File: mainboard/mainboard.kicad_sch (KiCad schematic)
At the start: 5 parts

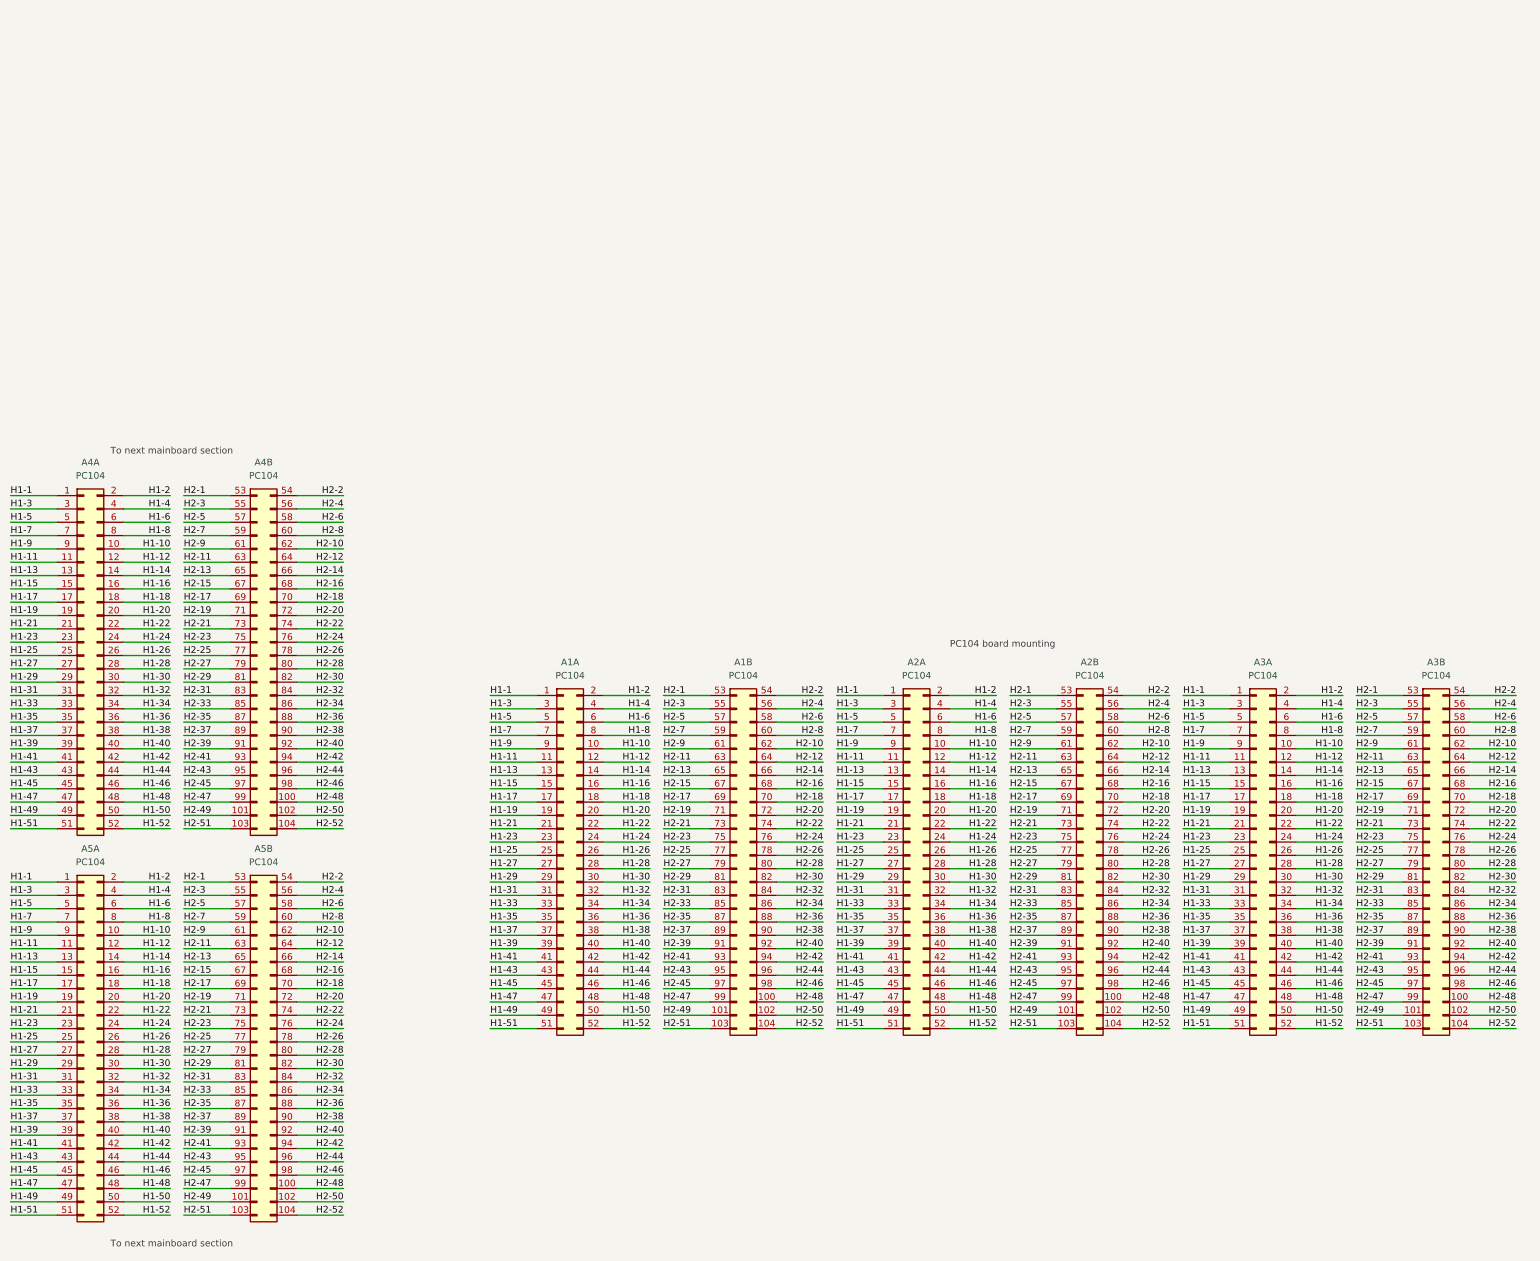
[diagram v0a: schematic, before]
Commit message: lay out the PC104 boards
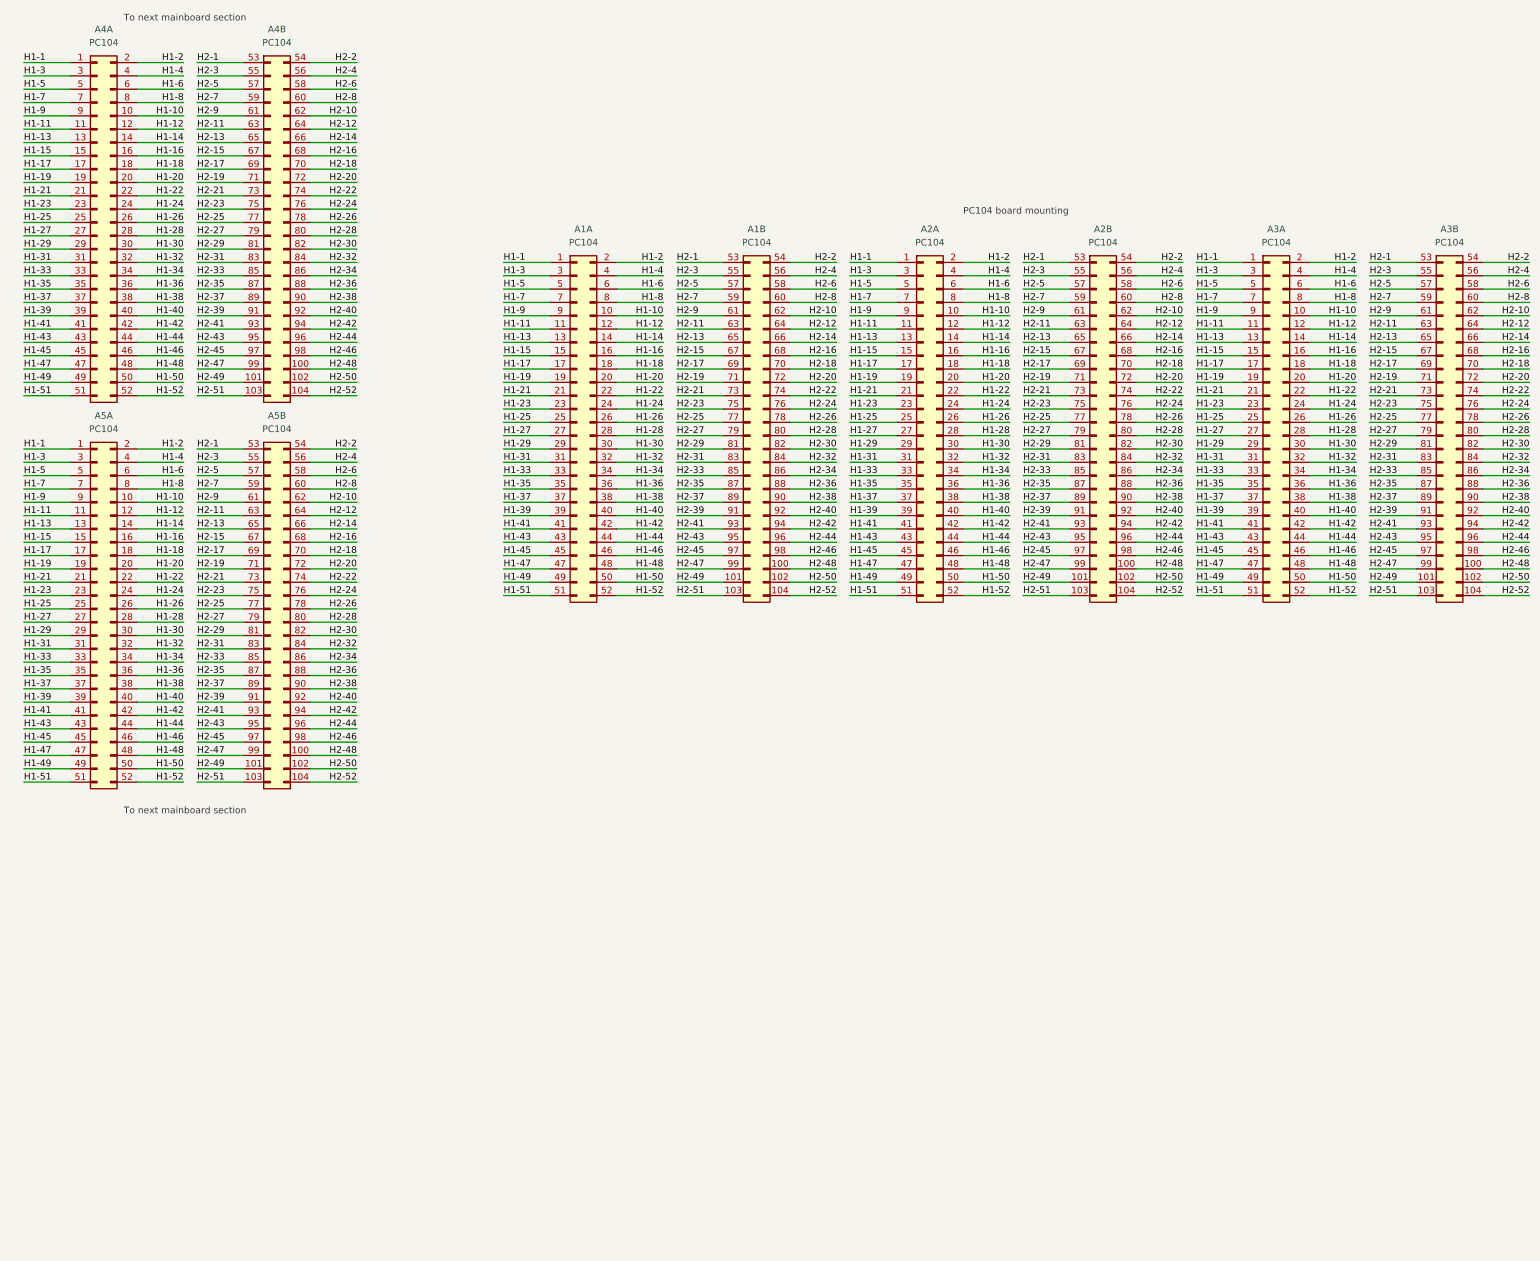
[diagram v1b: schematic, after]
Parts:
- A1, A2, A3: footprint (none) -> flatsat:PC104
- A4, A5: footprint (none) -> flatsat:Header
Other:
- moved on the sheet: A1A, A1B, A2A, A2B, A3A, A3B, A4A, A4B, A5A, A5B

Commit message: grounding
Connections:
- net H2-17 is gone; now on net GND: A1.69 (Pin_17), A2.69 (Pin_17), A3.69 (Pin_17), A4.69 (Pin_17), A5.69 (Pin_17)
- net H2-21 is gone; now on net GND: A1.73 (Pin_21), A2.73 (Pin_21), A3.73 (Pin_21), A4.73 (Pin_21), A5.73 (Pin_21)
- net H2-22 is gone; now on net GND: A1.74 (Pin_22), A2.74 (Pin_22), A3.74 (Pin_22), A4.74 (Pin_22), A5.74 (Pin_22)
- net H2-29 is gone; now on net GND: A1.81 (Pin_29), A2.81 (Pin_29), A3.81 (Pin_29), A4.81 (Pin_29), A5.81 (Pin_29)
- net H2-30 is gone; now on net GND: A1.82 (Pin_30), A2.82 (Pin_30), A3.82 (Pin_30), A4.82 (Pin_30), A5.82 (Pin_30)
- net H2-32 is gone; now on net GND: A1.84 (Pin_32), A2.84 (Pin_32), A3.84 (Pin_32), A4.84 (Pin_32), A5.84 (Pin_32)
- net H2-47 is gone; now on net GND: A1.99 (Pin_47), A2.99 (Pin_47), A3.99 (Pin_47), A4.99 (Pin_47), A5.99 (Pin_47)
- net H2-48 is gone; now on net GND: A1.100 (Pin_48), A2.100 (Pin_48), A3.100 (Pin_48), A4.100 (Pin_48), A5.100 (Pin_48)
- net H2-9 is gone; now on net GND: A1.61 (Pin_9), A2.61 (Pin_9), A3.61 (Pin_9), A4.61 (Pin_9), A5.61 (Pin_9)
- net H2-14 renamed GND

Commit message: bus power flags, finish left side routing
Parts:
- added H1, H2: MountingHole, MountingHole:MountingHole_3.2mm_M3, symbol Mechanical:MountingHole
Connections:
- net H2-26 is gone; now on net +5V: A1.78 (Pin_26), A2.78 (Pin_26), A3.78 (Pin_26), A4.78 (Pin_26), A5.78 (Pin_26)
- net H2-28 is gone; now on net +3V3: A1.80 (Pin_28), A2.80 (Pin_28), A3.80 (Pin_28), A4.80 (Pin_28), A5.80 (Pin_28)
- net H2-46 is gone; now on net +BATT: A1.98 (Pin_46), A2.98 (Pin_46), A3.98 (Pin_46), A4.98 (Pin_46), A5.98 (Pin_46)
- net GND: no longer A1.100 (Pin_48), A1.61 (Pin_9), A1.66 (Pin_14), A1.69 (Pin_17), A1.73 (Pin_21), A1.74 (Pin_22), A1.99 (Pin_47), A2.100 (Pin_48), A2.61 (Pin_9), A2.66 (Pin_14), A2.69 (Pin_17), A2.73 (Pin_21), A2.74 (Pin_22), A2.99 (Pin_47), A3.100 (Pin_48), A3.61 (Pin_9), A3.66 (Pin_14), A3.69 (Pin_17), A3.73 (Pin_21), A3.74 (Pin_22), A3.99 (Pin_47), A4.100 (Pin_48), A4.61 (Pin_9), A4.66 (Pin_14), A4.69 (Pin_17), A4.73 (Pin_21), A4.74 (Pin_22), A4.99 (Pin_47), A5.100 (Pin_48), A5.61 (Pin_9), A5.66 (Pin_14), A5.69 (Pin_17), A5.73 (Pin_21), A5.74 (Pin_22), A5.99 (Pin_47)
- net H2-25 renamed +5V
- net H2-27 renamed +3V3
- net H2-45 renamed +BATT
- new net H2-14: A1.66 (Pin_14), A2.66 (Pin_14), A3.66 (Pin_14), A4.66 (Pin_14), A5.66 (Pin_14)
- new net H2-17: A1.69 (Pin_17), A2.69 (Pin_17), A3.69 (Pin_17), A4.69 (Pin_17), A5.69 (Pin_17)
- new net H2-21: A1.73 (Pin_21), A2.73 (Pin_21), A3.73 (Pin_21), A4.73 (Pin_21), A5.73 (Pin_21)
- new net H2-22: A1.74 (Pin_22), A2.74 (Pin_22), A3.74 (Pin_22), A4.74 (Pin_22), A5.74 (Pin_22)
- new net H2-47: A1.99 (Pin_47), A2.99 (Pin_47), A3.99 (Pin_47), A4.99 (Pin_47), A5.99 (Pin_47)
- new net H2-48: A1.100 (Pin_48), A2.100 (Pin_48), A3.100 (Pin_48), A4.100 (Pin_48), A5.100 (Pin_48)
- new net H2-9: A1.61 (Pin_9), A2.61 (Pin_9), A3.61 (Pin_9), A4.61 (Pin_9), A5.61 (Pin_9)
